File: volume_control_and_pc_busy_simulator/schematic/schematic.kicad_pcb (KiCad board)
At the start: 2 copper layers, 97.5 x 44.5 mm, 8 parts, among them SW1 RotaryEncoder_Switch, SW2 SW_Push, SW3 SW_Push, U1 Sparkfun_Pro_Micro

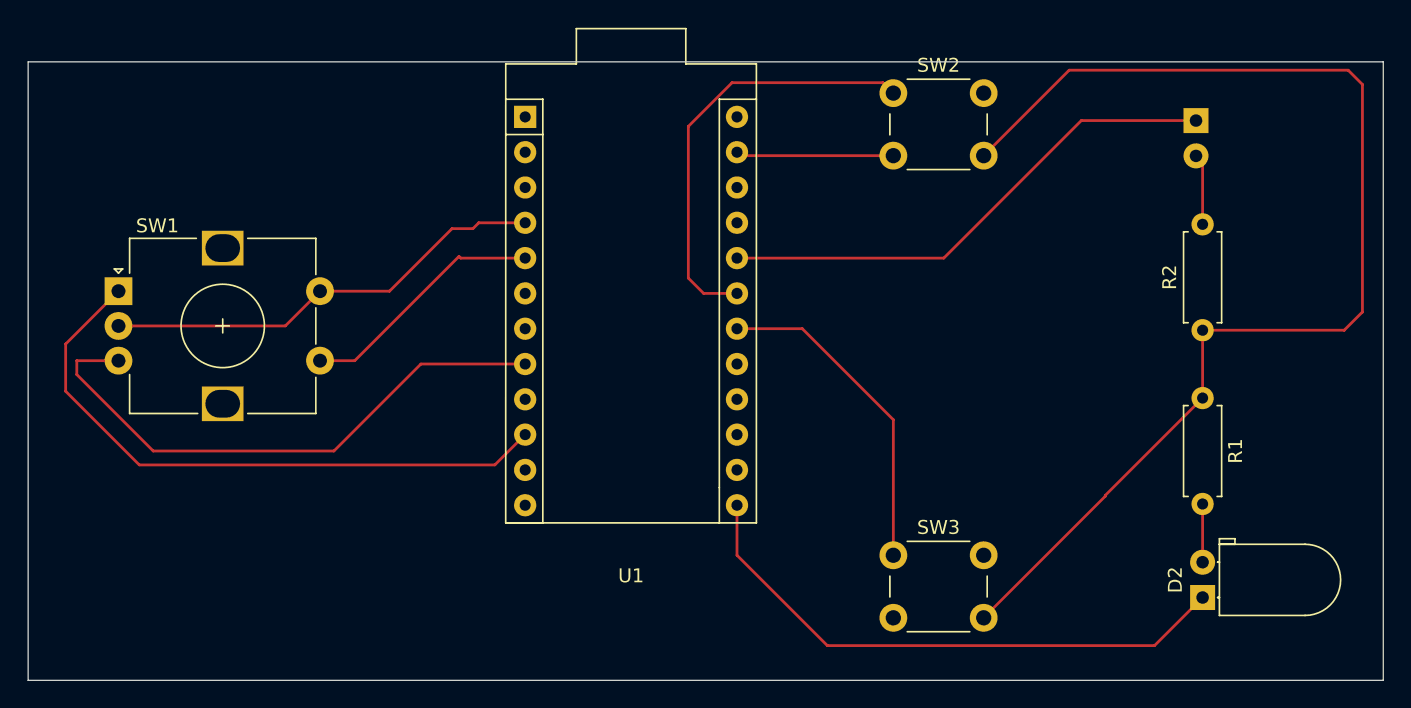
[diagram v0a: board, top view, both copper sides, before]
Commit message: VolumeControl: Schematic update
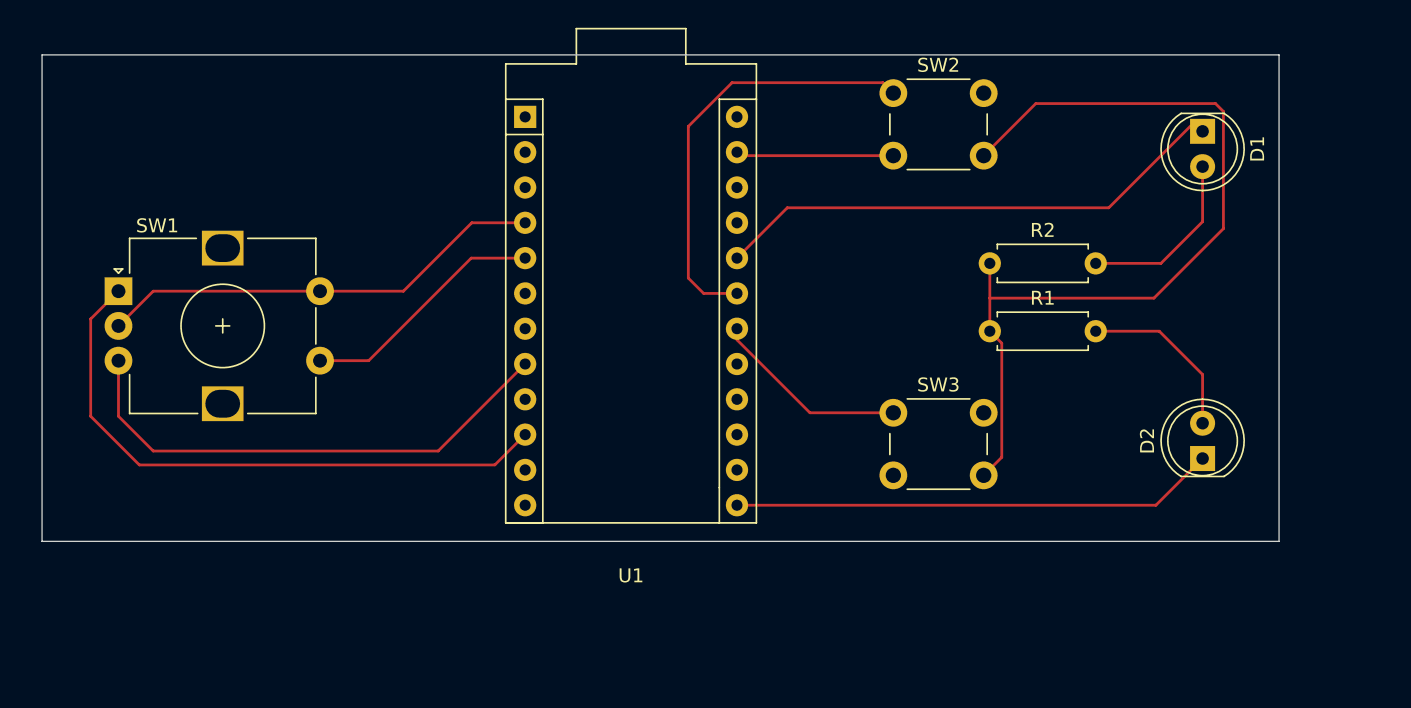
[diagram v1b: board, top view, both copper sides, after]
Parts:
- D1: footprint LED_THT:LED_D5.0mm_Horizontal_O1.27mm_Z15.0mm -> LED_THT:LED_D5.0mm; moved to F.Cu
- D2: footprint LED_THT:LED_D5.0mm_Horizontal_O1.27mm_Z15.0mm -> LED_THT:LED_D5.0mm
- moved R1 16.0 mm to (142.7, 76.4), turned to 0 degrees
- moved R2 16.0 mm to (142.7, 71.5), turned to 0 degrees
- moved SW3 10.2 mm to (135.8, 82.2)
- moved D2 10.0 mm to (158.0, 85.5)
- moved D1 0.91 mm to (158.0, 62.0)
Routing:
- net Net-(R1-Pad1): track 97.6 -> 74.2 mm
- net Net-(U1-D19/A1): track 23.7 -> 14.2 mm
- net Net-(D2-A): track 4.19 -> 12.5 mm
- net Net-(D1-A): track 5.12 -> 12.9 mm
- net Net-(D2-K): track 41.2 -> 34.9 mm
- net Net-(U1-~D5): track 41.1 -> 36.9 mm
- net Net-(U1-D7): track 44.9 -> 43.4 mm
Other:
- board size 97.5 x 44.5 mm -> 89 x 35 mm
